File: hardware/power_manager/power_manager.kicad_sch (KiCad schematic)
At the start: 14 parts, among them J1 Conn_01x02_Pin, J2 Conn_01x02_Pin, J3 Conn_01x02_Pin, U2 AP2112K-3.3, U3 TP4054-SOT25R

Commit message: Fix: Readme
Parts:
- added J4: USB_C_Receptacle_PowerOnly_6P, Connector_USB:USB_C_Receptacle_GCT_USB4125-xx-x_6P_TopMnt_Horizontal, symbol Connector:USB_C_Receptacle_PowerOnly_6P
- added R3, R4: 5.1k, symbol Device:R
- renumbered TP4 to TP3, U3 to U1
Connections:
- net GND: now also J4.A12 (GND), J4.B12 (GND), J4.SH (SHIELD), R3.2, R4.2
- net VIN: now reaches C2.1, D1.2 (A), J3.2 (Pin_2), U1.4 (V_{CC})
- net VIN: now also J4.A9 (VBUS), J4.B9 (VBUS)
- net VBAT: now reaches C1.1, J1.2 (Pin_2), TP1.1, U1.3 (BAT), U2.1 (VIN), U2.3 (EN)
- new net: J4.A5 (CC1), R4.1
- new net: J4.B5 (CC2), R3.1
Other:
- moved on the sheet: C1, C2, C3, D1, J1, J2, J3, R1, R2, TP1, TP2, TP3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

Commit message: Imp: Powermanager
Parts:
- removed J2: Conn_01x02_Pin, Connector_PinHeader_2.54mm:PinHeader_1x02_P2.54mm_Vertical, symbol Connector:Conn_01x02_Pin
- added C4: 100nF, Capacitor_THT:C_Disc_D6.0mm_W2.5mm_P5.00mm, symbol Device:C
- added D2: 1N5819, Diode_THT:D_DO-41_SOD81_P10.16mm_Horizontal, symbol Diode:1N5819
- added J2: Conn_01x03_Pin, Connector_PinHeader_2.54mm:PinHeader_1x03_P2.54mm_Vertical, symbol Connector:Conn_01x03_Pin
- added Q3: AO3401A, Package_TO_SOT_SMD:SOT-23, symbol Transistor_FET:AO3401A
- added R5: 1k, Resistor_THT:R_Axial_DIN0207_L6.3mm_D2.5mm_P10.16mm_Horizontal, symbol Device:R
- added R6: 5.1k, Resistor_THT:R_Axial_DIN0207_L6.3mm_D2.5mm_P10.16mm_Horizontal, symbol Device:R
- added R7, R8: 100k, Resistor_THT:R_Axial_DIN0207_L6.3mm_D2.5mm_P10.16mm_Horizontal, symbol Device:R
- R3, R4: footprint (none) -> Resistor_THT:R_Axial_DIN0207_L6.3mm_D2.5mm_P10.16mm_Horizontal
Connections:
- net GND: now also C4.2, J2.2 (Pin_2), R6.2, R8.2
- net VBAT: now also Q3.3 (D), R7.1; no longer U2.1 (VIN), U2.3 (EN)
- net VIN: now also D2.2 (A), R5.1
- net at C3.1, TP3.1, U2.5 (VOUT): now also J2.3 (Pin_3)
- new net: Q3.1 (G), R5.2, R6.1
- new net BAT_ADC: C4.1, J2.1 (Pin_1), R7.2, R8.1
- new net VCC: D2.1 (K), Q3.2 (S), U2.1 (VIN), U2.3 (EN)

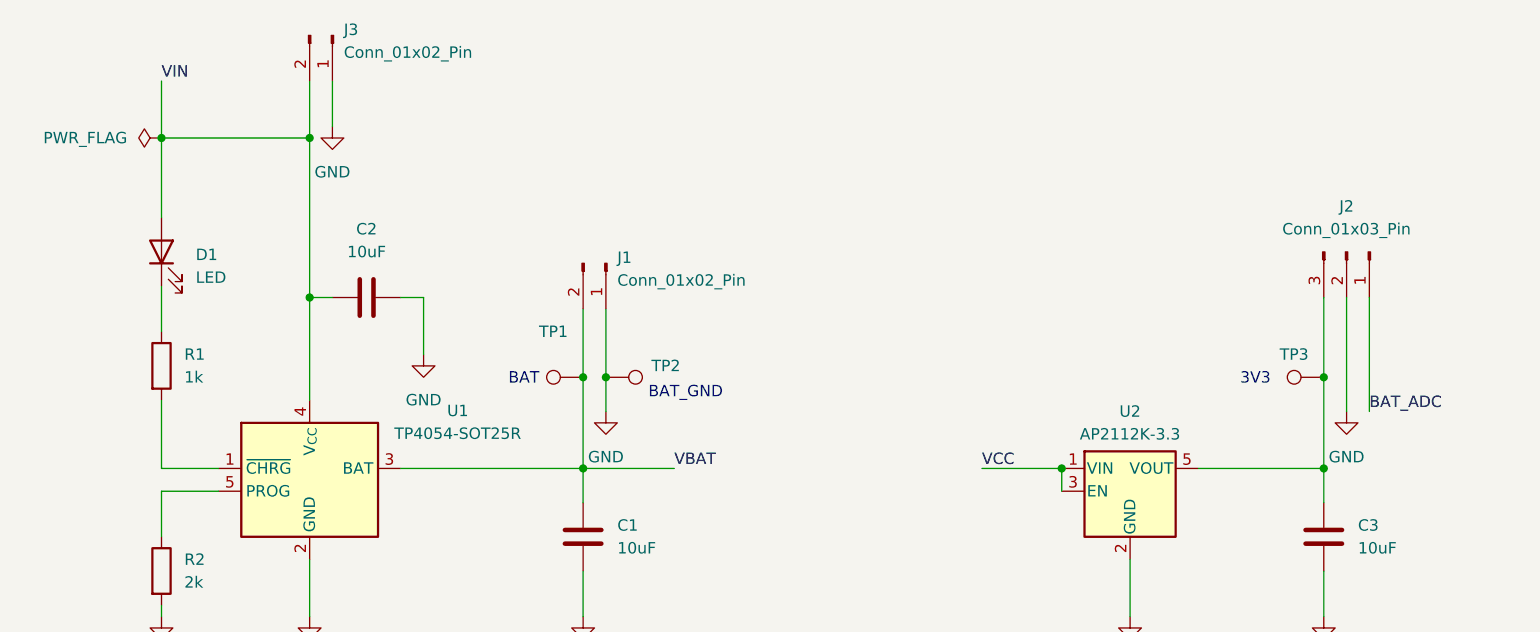
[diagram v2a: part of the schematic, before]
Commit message: Imp: powermanager schematic v0.2
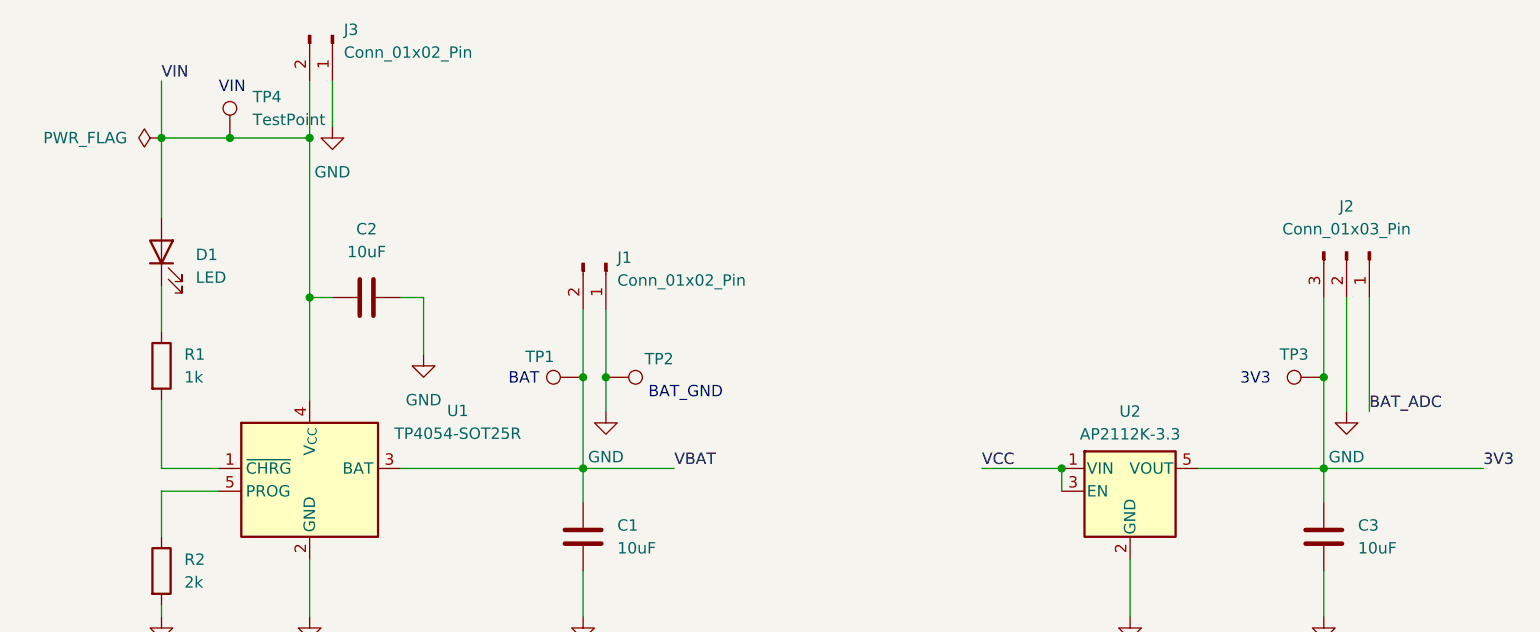
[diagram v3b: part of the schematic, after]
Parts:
- added TP4: TestPoint, TestPoint:TestPoint_Pad_D1.5mm, symbol Connector:TestPoint
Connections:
- net VIN: now also TP4.1
- net 3V3: now reaches C3.1, J2.3 (Pin_3), TP3.1, U2.5 (VOUT)
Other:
- note added: "VIN"
- title: (none) -> Cube Power Manager
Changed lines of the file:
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@@
 	(generator_version "10.0")
 	(paper "A4")
+	(title_block
+		(title "Cube Power Manager")
+		(date "2026-06-28")
+		(rev "v0.1")
+	)
 	(text "3V3"
 		(exclude_from_sim no)
@@
 		)
 	)
+	(text "VIN"
+		(exclude_from_sim no)
+		(at 106.934 26.162 0)
+		(effects
+			(font
+				(size 1.27 1.27)
+			)
+		)
+	)
 	(text "BAT_GND\n"
 		(exclude_from_sim no)
@@
 		(color 0 0 0 0)
 	)
+	(junction
+		(at 106.68 31.75)
+		(diameter 0)
+		(color 0 0 0 0)
+	)
 	(wire
 		(pts
@@
 	(wire
 		(pts
-			(xy 99.06 31.75) (xy 115.57 31.75)
+			(xy 99.06 31.75) (xy 106.68 31.75)
 		)
 		(stroke
@@
 	(wire
 		(pts
+			(xy 106.68 31.75) (xy 115.57 31.75)
+		)
+		(stroke
+			(width 0)
+			(type default)
+		)
+	)
+	(wire
+		(pts
 			(xy 88.9 134.62) (xy 88.9 107.95)
 		)
@@
 	(wire
 		(pts
+			(xy 228.6 68.58) (xy 246.38 68.58)
+		)
+		(stroke
+			(width 0)
+			(type default)
+		)
+	)
+	(wire
+		(pts
 			(xy 99.06 48.26) (xy 99.06 53.34)
 		)
@@
 		)
 	)
+	(label "3V3"
+		(at 246.38 68.58 0)
+		(effects
+			(font
+				(size 1.27 1.27)
+			)
+			(justify left bottom)
+		)
+	)
 	(label "VIN"
 		(at 99.06 25.4 0)
@@
 	)
 	(symbol
+		(lib_id "Connector:TestPoint")
+		(at 106.68 31.75 0)
+		(unit 1)
+		(body_style 1)
+		(exclude_from_sim no)
+		(in_bom yes)
+		(on_board yes)
+		(in_pos_files yes)
+		(dnp no)
+		(fields_autoplaced yes)
+		(property "Reference" "TP4"
+			(at 109.22 27.1779 0)
+			(show_name no)
+			(do_not_autoplace no)
+			(effects
+				(font
+					(size 1.27 1.27)
+				)
+				(justify left)
+			)
+		)
+		(property "Value" "TestPoint"
+			(at 109.22 29.7179 0)
+			(show_name no)
+			(do_not_autoplace no)
+			(effects
+				(font
+					(size 1.27 1.27)
+				)
+				(justify left)
+			)
+		)
+		(property "Footprint" "TestPoint:TestPoint_Pad_D1.5mm"
+			(at 111.76 31.75 0)
+			(hide yes)
+			(show_name no)
+			(do_not_autoplace no)
+			(effects
+				(font
+					(size 1.27 1.27)
+				)
+			)
+		)
+		(property "Datasheet" ""
+			(at 111.76 31.75 0)
+			(hide yes)
+			(show_name no)
+			(do_not_autoplace no)
+			(effects
+				(font
+					(size 1.27 1.27)
+				)
+			)
+		)
+		(property "Description" "test point"
+			(at 106.68 31.75 0)
+			(hide yes)
+			(show_name no)
+			(do_not_autoplace no)
+			(effects
+				(font
+					(size 1.27 1.27)
+				)
+			)
+		)
+		(pin "1"
+		)
+		(instances
+			(project "power_manager"
+				(path "/8494d822-bbbe-4c4e-b530-f67e3ef7c837"
+					(reference "TP4")
+					(unit 1)
+				)
+			)
+		)
+	)
+	(symbol
 		(lib_id "power:PWR_FLAG")
 		(at 99.06 31.75 90)
@@
 		(in_pos_files yes)
 		(dnp no)
-		(fields_autoplaced yes)
 		(property "Reference" "TP1"
-			(at 142.748 53.34 90)
+			(at 141.224 56.134 90)
 			(show_name no)
 			(do_not_autoplace no)
@@
 		(in_pos_files yes)
 		(dnp no)
-		(fields_autoplaced yes)
 		(property "Reference" "TP2"
-			(at 153.67 57.1499 90)
+			(at 152.908 56.388 90)
 			(show_name no)
 			(do_not_autoplace no)

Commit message: Add: PCB
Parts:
- removed J1, J3: Conn_01x02_Pin, Connector_PinHeader_2.54mm:PinHeader_1x02_P2.54mm_Vertical, symbol Connector:Conn_01x02_Pin
- removed J2: Conn_01x03_Pin, Connector_PinHeader_2.54mm:PinHeader_1x03_P2.54mm_Vertical, symbol Connector:Conn_01x03_Pin
- added C5, C7, C8: 100nF, Capacitor_SMD:C_0805_2012Metric, symbol Device:C
- added C6: 10uF, Capacitor_SMD:C_0805_2012Metric, symbol Device:C
- added D3: SMAJ5.0A, Diode_SMD:D_SMA, symbol Diode:SMAJ5.0A
- added D4: 1N5819, Diode_THT:D_DO-41_SOD81_P10.16mm_Horizontal, symbol Diode:1N5819
- added J5: Conn_01x08_Pin, Connector_PinHeader_2.54mm:PinHeader_1x08_P2.54mm_Vertical, symbol Connector:Conn_01x08_Pin
- added R10: 200k, Resistor_THT:R_Axial_DIN0207_L6.3mm_D2.5mm_P10.16mm_Horizontal, symbol Device:R
- added R11, R9: 1k, Resistor_THT:R_Axial_DIN0207_L6.3mm_D2.5mm_P10.16mm_Horizontal, symbol Device:R
- added R12: 300k, Resistor_THT:R_Axial_DIN0207_L6.3mm_D2.5mm_P10.16mm_Horizontal, symbol Device:R
- C1, C2, C4: footprint Capacitor_THT:C_Disc_D6.0mm_W2.5mm_P5.00mm -> Capacitor_SMD:C_0805_2012Metric
- C3: value 10uF -> 1uF; footprint Capacitor_THT:C_Disc_D6.0mm_W2.5mm_P5.00mm -> Capacitor_SMD:C_0805_2012Metric
- R7, R8: value 100k -> 470k
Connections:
- net 3V3: now also C7.2, J5.4 (Pin_4)
- net BAT_ADC: now also J5.2 (Pin_2), R9.1; no longer C4.1, R7.2, R8.1
- net GND: now also C5.2, C6.2, C7.1, C8.2, D3.2 (A2), J5.3 (Pin_3), J5.5 (Pin_5), J5.7 (Pin_7), R12.2
- net VBAT: now also D4.2 (A), J5.6 (Pin_6)
- net VCC: now also C6.1, D4.1 (K)
- net VIN: now also C5.1, D3.1 (A1), J5.8 (Pin_8), R10.1
- new net: C8.1, R10.2, R11.2, R12.1
- new net: C4.1, R7.2, R8.1, R9.2
- new net PLUGIN: J5.1 (Pin_1), R11.1
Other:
- note added: "GND"
- note removed: "BAT_GND"
- moved on the sheet: C2, C3, TP1, TP2, TP3, U2
